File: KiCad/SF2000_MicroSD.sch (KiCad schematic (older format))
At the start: 4 parts, among them J6 Micro_SD_Card_Socket, X1 Oscillator_7.0x5.0mm

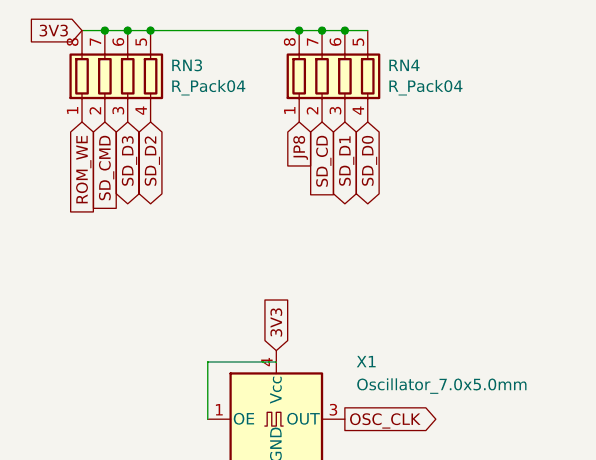
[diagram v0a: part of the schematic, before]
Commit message: Re-routed for a GoWin FPGA GW1N-UV9LQ144 (or GW1N-UV4LQ144) and added a Pmod type 2A SPI-header.
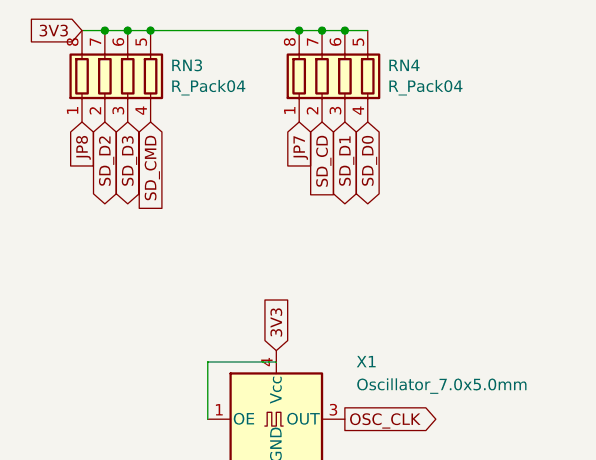
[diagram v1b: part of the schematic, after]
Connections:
- net labels added: JP7
- net labels removed: ROM_WE
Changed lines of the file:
@@
 Wire Wire Line
 	3150 2800 3250 2800
-Text GLabel 2300 3200 3    50   BiDi ~ 0
+Text GLabel 2100 3200 3    50   BiDi ~ 0
 SD_D2
 Text GLabel 2200 3200 3    50   BiDi ~ 0
 SD_D3
-Text GLabel 2100 3200 3    50   Input ~ 0
+Text GLabel 2300 3200 3    50   Input ~ 0
 SD_CMD
 Text GLabel 3250 3200 3    50   BiDi ~ 0
@@
 Text GLabel 3150 4500 2    50   Output ~ 0
 OSC_CLK
+Text GLabel 2000 3200 3    50   Input ~ 0
+JP8
 Text GLabel 2950 3200 3    50   Input ~ 0
-JP8
-Text GLabel 2000 3200 3    50   Input ~ 0
-ROM_WE
+JP7
 $EndSCHEMATC

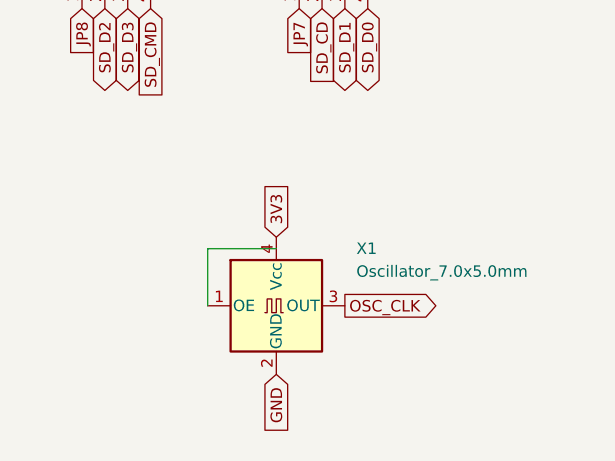
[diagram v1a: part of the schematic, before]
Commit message: removed CDAC-signal (not needed) and assigned E-signal to pin 11 (GCLKT_7) instead
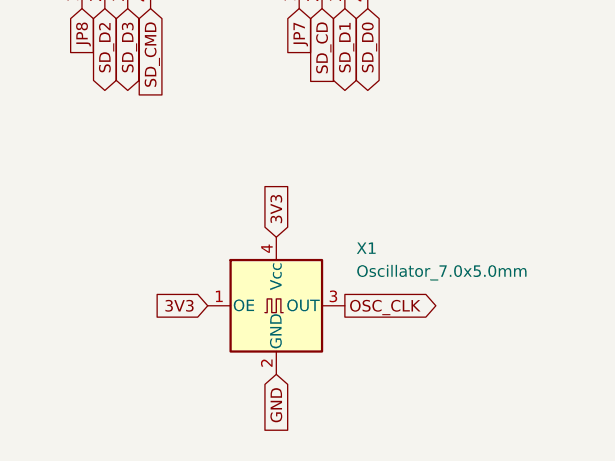
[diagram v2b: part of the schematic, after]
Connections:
- wire segments 9 -> 7
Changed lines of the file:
@@
 Text GLabel 2850 4800 3    50   Input ~ 0
 GND
-Wire Wire Line
-	2850 4250 2550 4250
-Wire Wire Line
-	2550 4250 2550 4500
 Text GLabel 3150 4500 2    50   Output ~ 0
 OSC_CLK
@@
 Text GLabel 2950 3200 3    50   Input ~ 0
 JP7
+Text GLabel 2550 4500 0    50   Input ~ 0
+3V3
 $EndSCHEMATC

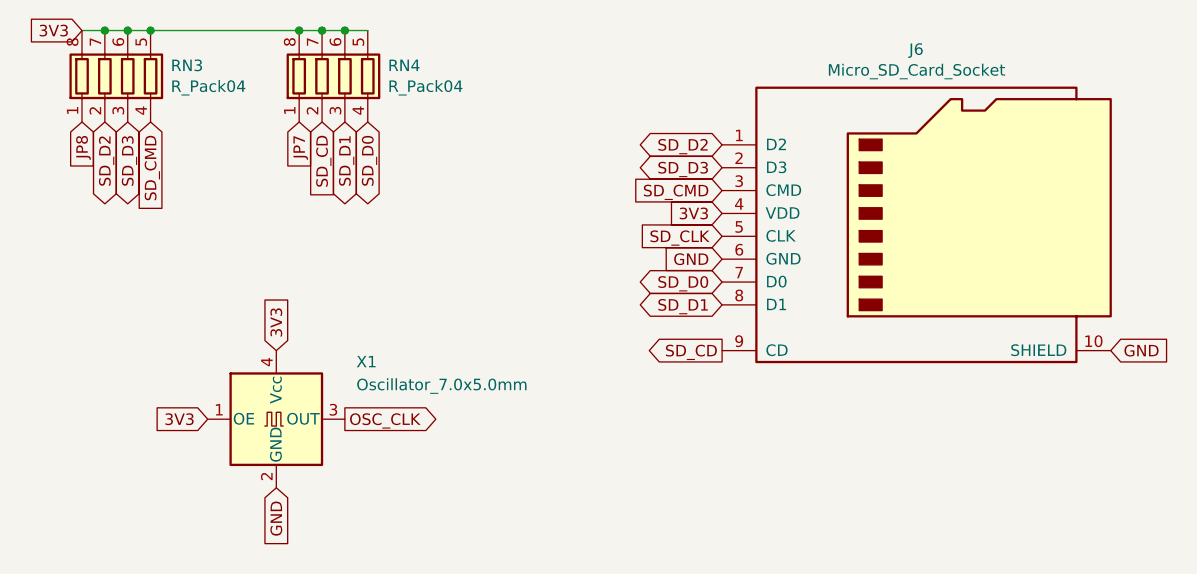
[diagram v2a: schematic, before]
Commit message: Change R10 to 33 Ohm and used with crystal oscillator
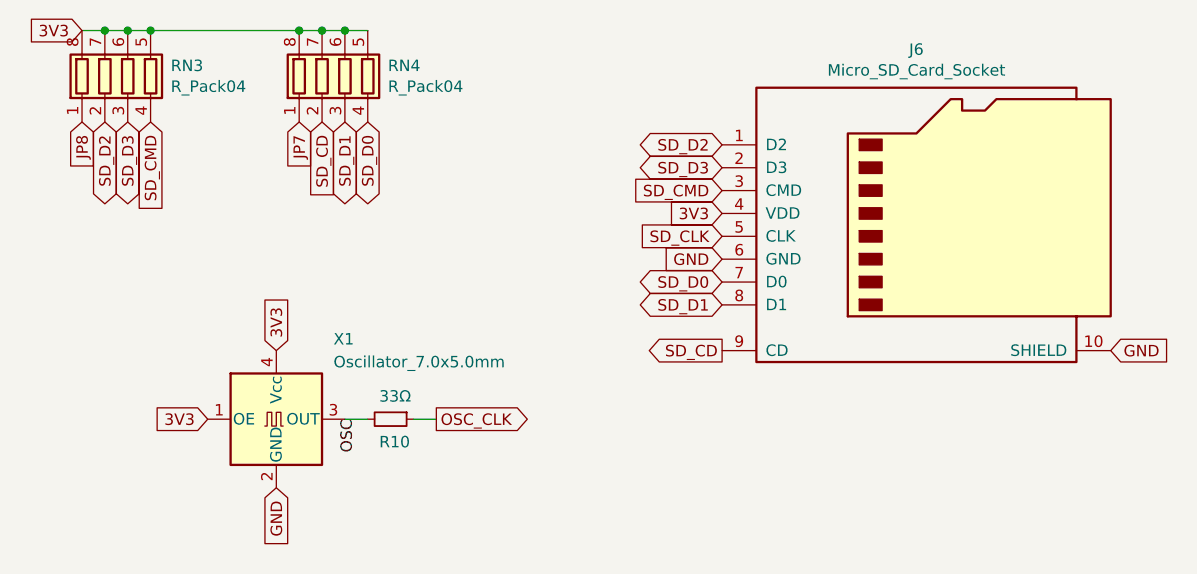
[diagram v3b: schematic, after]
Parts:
- added R10: 33Ω, Resistor_SMD:R_0805_2012Metric_Pad1.20x1.40mm_HandSolder, symbol Device:R_Small
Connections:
- net OSC_CLK: now also R10.1; no longer X1.3 (OUT)
- new net OSC: R10.2, X1.3 (OUT)
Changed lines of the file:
@@
 U 1 1 620EE0AB
 P 2850 4500
-F 0 "X1" H 3200 4750 50  0000 L CNN
-F 1 "Oscillator_7.0x5.0mm" H 3200 4650 50  0000 L CNN
+F 0 "X1" H 3100 4850 50  0000 L CNN
+F 1 "Oscillator_7.0x5.0mm" H 3100 4750 50  0000 L CNN
 F 2 "Oscillator:Oscillator_SMD_SeikoEpson_SG8002CA-4Pin_7.0x5.0mm" H 3550 4150 50  0001 C CNN
 F 3 "" H 2750 4500 50  0001 C CNN
@@
 Text GLabel 2850 4800 3    50   Input ~ 0
 GND
-Text GLabel 3150 4500 2    50   Output ~ 0
+Text GLabel 3550 4500 2    50   Output ~ 0
 OSC_CLK
 Text GLabel 2000 3200 3    50   Input ~ 0
@@
 Text GLabel 2550 4500 0    50   Input ~ 0
 3V3
+$Comp
+L Device:R_Small R?
+U 1 1 68B856DF
+P 3350 4500
+AR Path="/68B856DF" Ref="R?"  Part="1"
+AR Path="/620D263D/68B856DF" Ref="R?"  Part="1"
+AR Path="/62892CF3/68B856DF" Ref="R10"  Part="1"
+F 0 "R10" V 3450 4450 50  0000 L CNN
+F 1 "33Ω" V 3250 4450 50  0000 L CNN
+F 2 "Resistor_SMD:R_0805_2012Metric_Pad1.20x1.40mm_HandSolder" H 3350 4500 50  0001 C CNN
+F 3 "~" H 3350 4500 50  0001 C CNN
+	1    3350 4500
+	0    1    1    0
+$EndComp
+Wire Wire Line
+	3550 4500 3450 4500
+Wire Wire Line
+	3250 4500 3150 4500
+Text Label 3200 4500 3    50   ~ 0
+OSC
 $EndSCHEMATC

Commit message: Fixed enumeration of single resistors references in ascending order
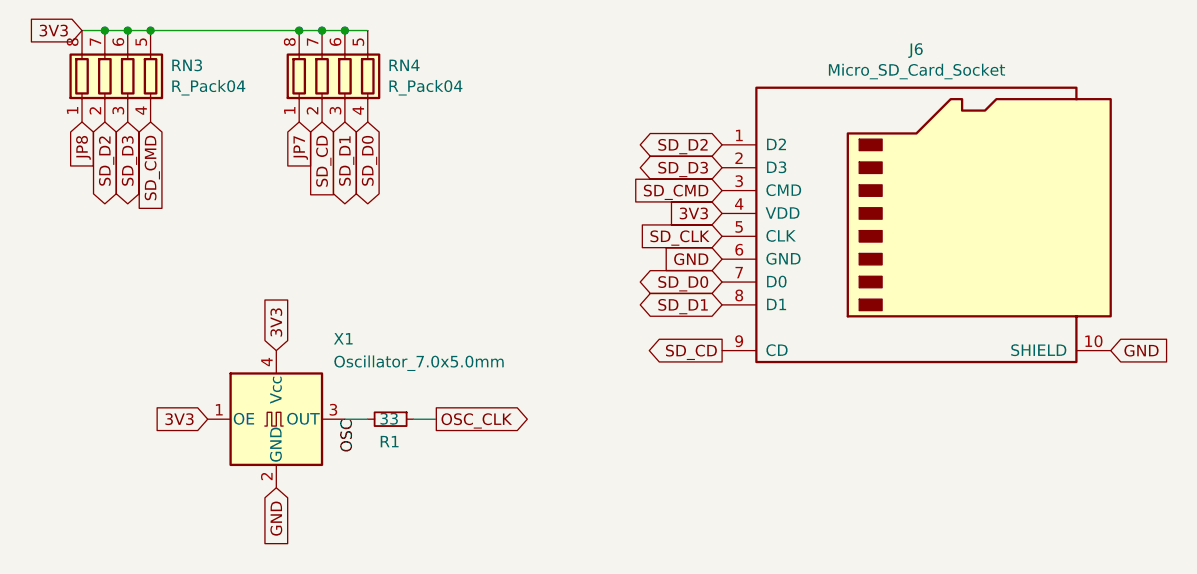
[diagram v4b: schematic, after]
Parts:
- R1: renamed from R10; value 33Ω -> 33
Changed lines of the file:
@@
 AR Path="/68B856DF" Ref="R?"  Part="1"
 AR Path="/620D263D/68B856DF" Ref="R?"  Part="1"
-AR Path="/62892CF3/68B856DF" Ref="R10"  Part="1"
-F 0 "R10" V 3450 4450 50  0000 L CNN
-F 1 "33Ω" V 3250 4450 50  0000 L CNN
+AR Path="/62892CF3/68B856DF" Ref="R1"  Part="1"
+F 0 "R1" V 3450 4450 50  0000 L CNN
+F 1 "33" V 3350 4450 50  0000 L CNN
 F 2 "Resistor_SMD:R_0805_2012Metric_Pad1.20x1.40mm_HandSolder" H 3350 4500 50  0001 C CNN
 F 3 "~" H 3350 4500 50  0001 C CNN

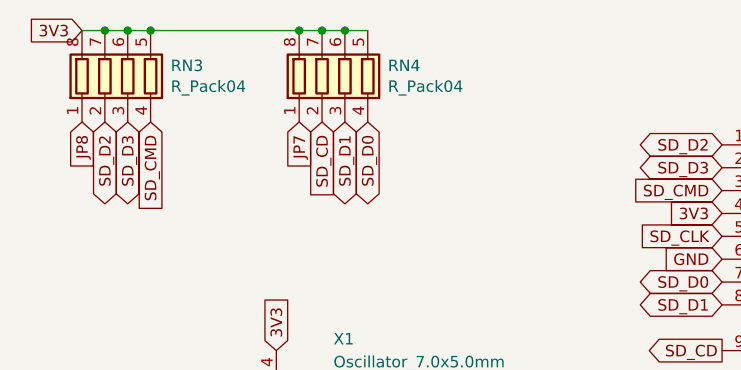
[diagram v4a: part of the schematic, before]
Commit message: Adding RN6 pull-up resistor, Routing of A15-A6 to FPGA and more cleanup
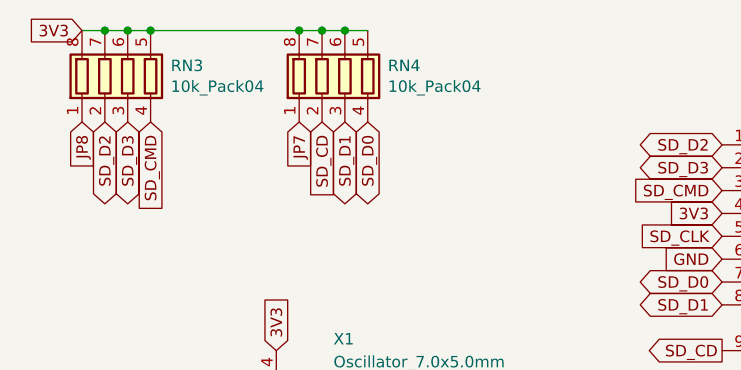
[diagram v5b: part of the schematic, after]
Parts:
- RN3, RN4: value R_Pack04 -> 10k_Pack04
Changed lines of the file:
@@
 P 2200 3000
 F 0 "RN3" H 2388 3046 50  0000 L CNN
-F 1 "R_Pack04" H 2388 2955 50  0000 L CNN
+F 1 "10k_Pack04" H 2388 2955 50  0000 L CNN
 F 2 "SF2000:RESCAF80P320X160X60-8N" V 2475 3000 50  0001 C CNN
 F 3 "~" H 2200 3000 50  0001 C CNN
@@
 P 3150 3000
 F 0 "RN4" H 3338 3046 50  0000 L CNN
-F 1 "R_Pack04" H 3338 2955 50  0000 L CNN
+F 1 "10k_Pack04" H 3338 2955 50  0000 L CNN
 F 2 "SF2000:RESCAF80P320X160X60-8N" V 3425 3000 50  0001 C CNN
 F 3 "~" H 3150 3000 50  0001 C CNN

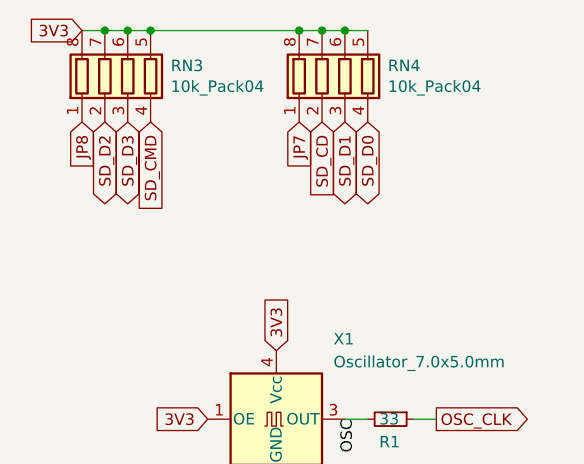
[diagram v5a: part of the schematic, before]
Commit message: Add SD_LED & LED Activity circuit and small fixes and routing around the clockport area
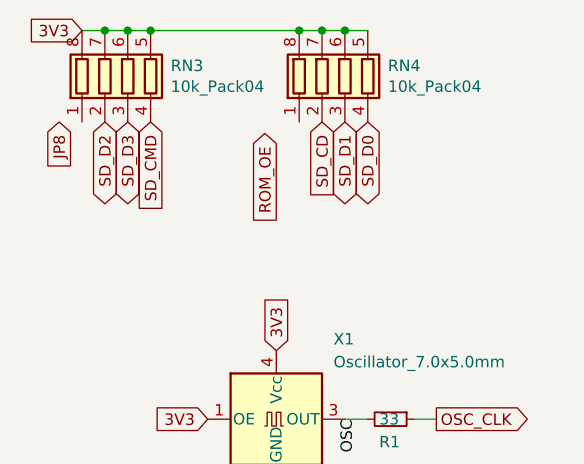
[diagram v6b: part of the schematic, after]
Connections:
- net JP8: no longer RN3.1 (R1.1)
- net JP7: no longer names the net of RN4.1 (R1.1)
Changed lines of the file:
@@
 Text GLabel 3550 4500 2    50   Output ~ 0
 OSC_CLK
-Text GLabel 2000 3200 3    50   Input ~ 0
+Text GLabel 1900 3200 3    50   Input ~ 0
 JP8
-Text GLabel 2950 3200 3    50   Input ~ 0
-JP7
 Text GLabel 2550 4500 0    50   Input ~ 0
 3V3
@@
 Text Label 3200 4500 3    50   ~ 0
 OSC
+Text GLabel 2800 3250 3    50   Input ~ 0
+ROM_OE
 $EndSCHEMATC

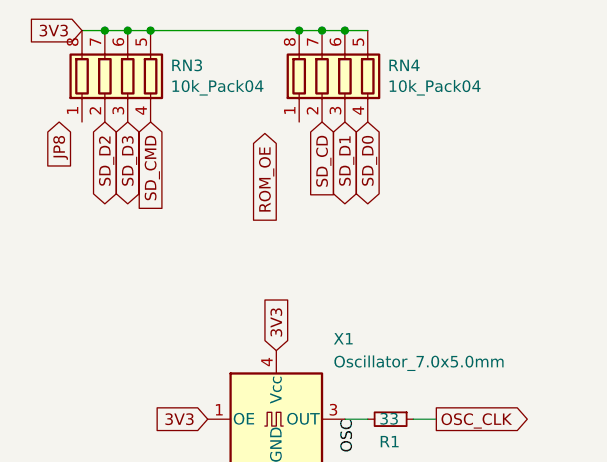
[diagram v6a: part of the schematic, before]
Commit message: Fixed routing D0-D7 lines plus some cleanup and routing of power supply to FPGA power pins
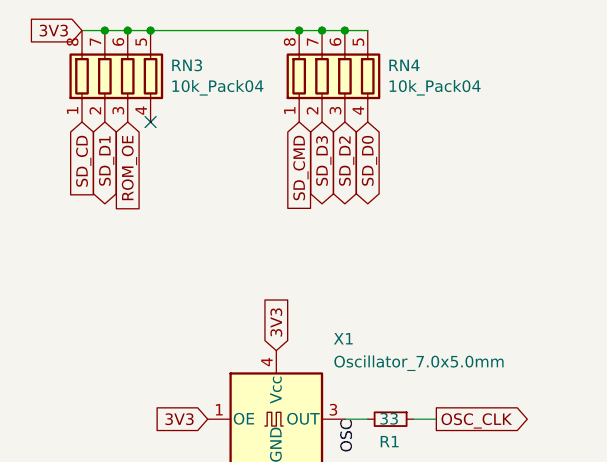
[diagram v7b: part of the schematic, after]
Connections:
- net ROM_OE: now also RN3.3 (R3.1)
- net SD_CD: now also RN3.1 (R1.1); no longer RN4.2 (R2.1)
- net SD_CMD: now also RN4.1 (R1.1); no longer RN3.4 (R4.1)
- net SD_D1: now also RN3.2 (R2.1); no longer RN4.3 (R3.1)
- net SD_D2: now also RN4.3 (R3.1); no longer RN3.2 (R2.1)
- net SD_D3: now also RN4.2 (R2.1); no longer RN3.3 (R3.1)
- no-connect marks 0 -> 1
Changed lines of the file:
@@
 Wire Wire Line
 	3150 2800 3250 2800
-Text GLabel 2100 3200 3    50   BiDi ~ 0
+Text GLabel 3150 3200 3    50   BiDi ~ 0
 SD_D2
-Text GLabel 2200 3200 3    50   BiDi ~ 0
+Text GLabel 3050 3200 3    50   BiDi ~ 0
 SD_D3
-Text GLabel 2300 3200 3    50   Input ~ 0
+Text GLabel 2950 3200 3    50   Input ~ 0
 SD_CMD
 Text GLabel 3250 3200 3    50   BiDi ~ 0
 SD_D0
-Text GLabel 3150 3200 3    50   BiDi ~ 0
+Text GLabel 2100 3200 3    50   BiDi ~ 0
 SD_D1
-Text GLabel 3050 3200 3    50   Input ~ 0
+Text GLabel 2000 3200 3    50   Input ~ 0
 SD_CD
 $Comp
@@
 Text GLabel 3550 4500 2    50   Output ~ 0
 OSC_CLK
-Text GLabel 1900 3200 3    50   Input ~ 0
-JP8
 Text GLabel 2550 4500 0    50   Input ~ 0
 3V3
@@
 Text Label 3200 4500 3    50   ~ 0
 OSC
-Text GLabel 2800 3250 3    50   Input ~ 0
+Text GLabel 2200 3200 3    50   Input ~ 0
 ROM_OE
+NoConn ~ 2300 3200
 $EndSCHEMATC

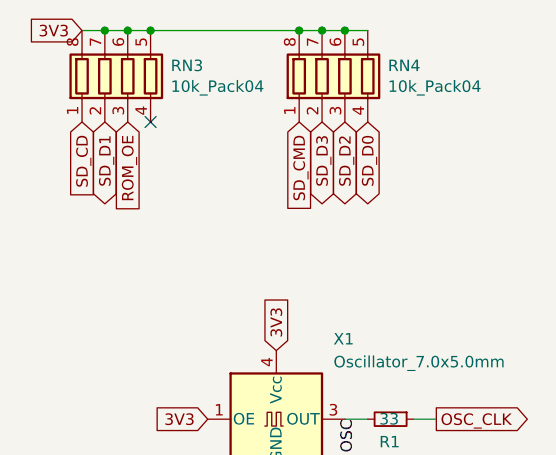
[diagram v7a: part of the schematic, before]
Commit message: Fixed driver bank select jumper for ROM at U14, pulled-up by vacant resistor in RN3
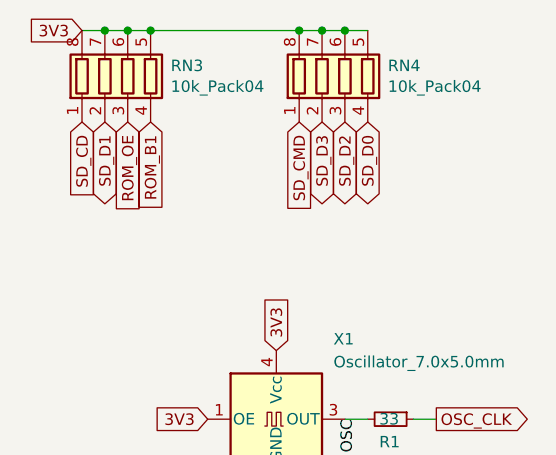
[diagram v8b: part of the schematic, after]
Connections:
- net ROM_B1: now reaches RN3.4 (R4.1)
- no-connect marks 1 -> 0
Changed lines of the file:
@@
 Text GLabel 2200 3200 3    50   Input ~ 0
 ROM_OE
-NoConn ~ 2300 3200
+Text GLabel 2300 3200 3    50   Input ~ 0
+ROM_B1
 $EndSCHEMATC
